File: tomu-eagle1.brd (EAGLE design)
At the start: 14.4 x 9.7 mm, 18 parts, among them U1 EFM32HG309F64G

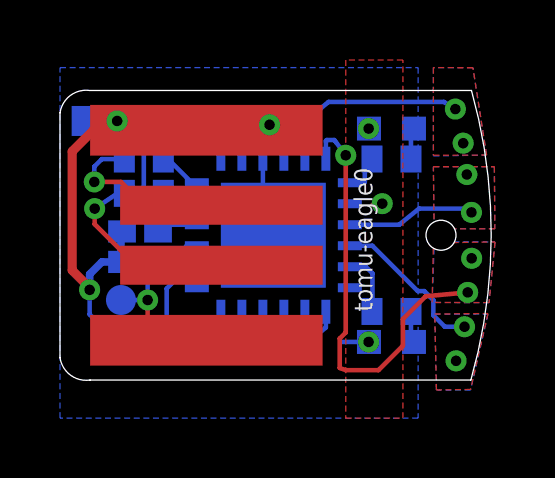
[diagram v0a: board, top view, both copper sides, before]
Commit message: added tomu-eagle1, more faithful to original tomu 0.4
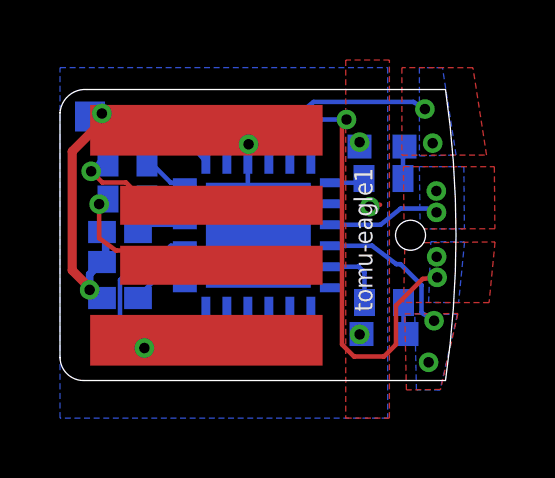
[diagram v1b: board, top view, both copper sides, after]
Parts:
- moved 5V 1.61 mm to (1.68, 2.12), turned to 180 degrees
- moved C1 1.24 mm to (2.00, 3.75)
- moved R1 0.70 mm to (10.8, 7.73)
- moved LED2 0.68 mm to (10.7, 8.80)
- moved C2 0.67 mm to (2.00, 5.95)
- moved C3 0.67 mm to (2.00, 4.95)
- moved R3 0.58 mm to (2.25, 7.05)
- moved R4 0.56 mm to (2.25, 8.25)
- moved U1 0.50 mm to (6.61, 5.84)
- moved D 0.41 mm to (5.57, 9.62)
- moved R2 0.39 mm to (10.8, 3.60)
- moved LED1 0.36 mm to (10.8, 2.55)
- moved C 0.19 mm to (3.27, 9.62)
- moved - 0.19 mm to (1.00, 9.80)
- moved R 0.10 mm to (4.83, 2.06)
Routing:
- net GND: track 25.6 -> 21.0 mm
- net DECOUPLE: track 3.30 -> 2.28 mm
- net +3V3: track 6.05 -> 5.12 mm
- net DBG_SWCLK: track 3.02 -> 2.14 mm
- net CAP1B: track 14.6 -> 15.4 mm
- net VUSB: track 7.46 -> 8.16 mm
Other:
- board size 14.4 x 9.7 mm -> 13.2 x 9.7 mm
- board text added: "tomu-eagle1"
- board text removed: "tomu-eagle0"

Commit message: fixes to tomu-eagle1
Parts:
- C1: device adafruit:C0402K -> adafruit:C0402
- moved LED1 0.05 mm to (10.8, 2.55)
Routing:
- net CAP1B: track 15.4 -> 14.3 mm
- net CAP0B: track 6.14 -> 6.26 mm, vias 2 -> 3
- net CAP1A: vias 2 -> 3
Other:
- outline, holes or cut-outs redrawn

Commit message: more fixes to tomu-eagle1
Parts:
- moved R2 0.21 mm to (10.8, 3.80)
- moved LED1 0.20 mm to (10.8, 2.75)

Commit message: more fixes, update readme
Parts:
- C2, C3: device adafruit:C0402K -> adafruit:C0402
- moved 5V 0.60 mm to (1.08, 2.12)
- moved C1 0.20 mm to (2.00, 3.55)
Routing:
- net VUSB: track 8.16 -> 8.71 mm
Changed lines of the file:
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@@
 <layer number="28" name="bValues" color="7" fill="1" visible="no" active="yes"/>
 <layer number="29" name="tStop" color="7" fill="3" visible="no" active="yes"/>
-<layer number="30" name="bStop" color="7" fill="6" visible="no" active="yes"/>
+<layer number="30" name="bStop" color="7" fill="6" visible="yes" active="yes"/>
 <layer number="31" name="tCream" color="7" fill="4" visible="no" active="yes"/>
 <layer number="32" name="bCream" color="7" fill="5" visible="no" active="yes"/>
@@
 <hole x="11.684" y="5.842" drill="1.2"/>
 <polygon width="0.1524" layer="29">
-<vertex x="12.192" y="11.684"/>
+<vertex x="11.392" y="11.684"/>
 <vertex x="14.986" y="11.684"/>
 <vertex x="14.986" y="0"/>
-<vertex x="12.192" y="0"/>
+<vertex x="11.392" y="0"/>
 </polygon>
 <polygon width="0.1524" layer="30">
@@
 </autorouter>
 <elements>
-<element name="C1" library="adafruit" library_urn="urn:adsk.eagle:library:420" package="C0402" value="1uF" x="2" y="3.75" smashed="yes" rot="MR0">
-<attribute name="NAME" x="0.922" y="3.463" size="0.6096" layer="26" ratio="12" rot="MR0"/>
-<attribute name="VALUE" x="2.5" y="2.3" size="1.016" layer="28" rot="MR0"/>
-</element>
-<element name="C2" library="adafruit" library_urn="urn:adsk.eagle:library:420" package="C0402K" value="1uF" x="2" y="5.95" smashed="yes" rot="MR0">
+<element name="C1" library="adafruit" library_urn="urn:adsk.eagle:library:420" package="C0402" value="1uF" x="2" y="3.55" smashed="yes" rot="MR0">
+<attribute name="NAME" x="0.922" y="3.063" size="0.6096" layer="26" ratio="12" rot="MR0"/>
+<attribute name="VALUE" x="2.5" y="2.1" size="1.016" layer="28" rot="MR0"/>
+</element>
+<element name="C2" library="adafruit" library_urn="urn:adsk.eagle:library:420" package="C0402" value="1uF" x="2" y="5.95" smashed="yes" rot="MR0">
 <attribute name="NAME" x="0.872" y="5.613" size="0.6096" layer="26" ratio="12" rot="MR0"/>
 <attribute name="VALUE" x="2.5" y="4.5" size="1.016" layer="28" rot="MR0"/>
 </element>
-<element name="C3" library="adafruit" library_urn="urn:adsk.eagle:library:420" package="C0402K" value="4.7uF" x="2" y="4.95" smashed="yes" rot="MR0">
-<attribute name="NAME" x="0.872" y="4.663" size="0.6096" layer="26" ratio="12" rot="MR0"/>
-<attribute name="VALUE" x="2.5" y="3.5" size="1.016" layer="28" rot="MR0"/>
+<element name="C3" library="adafruit" library_urn="urn:adsk.eagle:library:420" package="C0402" value="4.7uF" x="2" y="4.9" smashed="yes" rot="MR0">
+<attribute name="NAME" x="0.872" y="4.613" size="0.6096" layer="26" ratio="12" rot="MR0"/>
+<attribute name="VALUE" x="2.5" y="3.45" size="1.016" layer="28" rot="MR0"/>
 </element>
 <element name="LED1" library="adafruit" library_urn="urn:adsk.eagle:library:420" package="CHIP-LED0603" value="grn" x="10.75" y="2.75" smashed="yes" rot="MR90">
@@
 </element>
 <element name="R3" library="adafruit" library_urn="urn:adsk.eagle:library:420" package="R0402" value="15" x="2.25" y="7.05" smashed="yes" rot="MR0">
-<attribute name="NAME" x="1.207" y="6.796" size="0.6096" layer="26" ratio="12" rot="MR0"/>
+<attribute name="NAME" x="1.207" y="6.996" size="0.6096" layer="26" ratio="12" rot="MR0"/>
 </element>
 <element name="R4" library="adafruit" library_urn="urn:adsk.eagle:library:420" package="R0402" value="15" x="2.25" y="8.25" smashed="yes" rot="MR0">
-<attribute name="NAME" x="1.157" y="7.996" size="0.6096" layer="26" ratio="12" rot="MR0"/>
+<attribute name="NAME" x="1.157" y="8.196" size="0.6096" layer="26" ratio="12" rot="MR0"/>
 </element>
 <element name="U1" library="todstuff" package="QFN24PAD" value="EFM32HG309F64G" x="6.612" y="5.842" smashed="yes" rot="MR0">
@@
 </element>
 <element name="T" library="testpad" library_urn="urn:adsk.eagle:library:385" package="TP10R" package3d_urn="urn:adsk.eagle:package:27959/1" value="TPTP10R" x="6.604" y="2.109" smashed="yes" rot="MR0">
-<attribute name="NAME" x="6.015" y="1.4931" size="0.8128" layer="26" ratio="12" rot="MR0"/>
+<attribute name="NAME" x="6" y="1.6" size="0.8128" layer="26" ratio="12" rot="MR0"/>
 <attribute name="TP_SIGNAL_NAME" value="" x="6.604" y="0.204" size="1" layer="38" rot="MR0"/>
 </element>
 <element name="R" library="testpad" library_urn="urn:adsk.eagle:library:385" package="TP10R" package3d_urn="urn:adsk.eagle:package:27959/1" value="TPTP10R" x="4.826" y="2.059" smashed="yes" rot="MR0">
-<attribute name="NAME" x="3.983" y="1.4431" size="0.8128" layer="26" ratio="12" rot="MR0"/>
+<attribute name="NAME" x="4" y="1.6" size="0.8128" layer="26" ratio="12" rot="MR0"/>
 <attribute name="TP_SIGNAL_NAME" value="" x="4.826" y="0.154" size="1" layer="38" rot="MR0"/>
 </element>
@@
 </element>
 <element name="RS" library="testpad" library_urn="urn:adsk.eagle:library:385" package="TP10R" package3d_urn="urn:adsk.eagle:package:27959/1" value="TPTP10R" x="8.128" y="2.109" smashed="yes" rot="MR90">
-<attribute name="NAME" x="9.571" y="1.7471" size="0.6096" layer="26" ratio="12" rot="MR0"/>
+<attribute name="NAME" x="8.629" y="3.0529" size="0.6096" layer="26" ratio="12" rot="MR180"/>
 <attribute name="TP_SIGNAL_NAME" value="" x="6.223" y="2.109" size="1" layer="38" rot="MR90"/>
 </element>
-<element name="5V" library="testpad" library_urn="urn:adsk.eagle:library:385" package="TP10R" package3d_urn="urn:adsk.eagle:package:27959/1" value="TPTP10R" x="1.676" y="2.117" smashed="yes" rot="MR180">
-<attribute name="NAME" x="0.029" y="2.6789" size="0.8128" layer="26" ratio="12" rot="MR180"/>
-<attribute name="TP_SIGNAL_NAME" value="" x="1.676" y="4.022" size="1" layer="38" rot="MR180"/>
-<attribute name="VALUE" x="1.295" y="2.498" size="0.0254" layer="28" rot="MR180"/>
+<element name="5V" library="testpad" library_urn="urn:adsk.eagle:library:385" package="TP10R" package3d_urn="urn:adsk.eagle:package:27959/1" value="TPTP10R" x="1.076" y="2.117" smashed="yes" rot="MR180">
+<attribute name="NAME" x="2.85" y="1.8" size="0.75" layer="26" ratio="12" rot="MR0"/>
+<attribute name="TP_SIGNAL_NAME" value="" x="1.076" y="4.022" size="1" layer="38" rot="MR180"/>
+<attribute name="VALUE" x="0.695" y="2.498" size="0.0254" layer="28" rot="MR180"/>
 </element>
 <element name="U$1" library="todstuff" package="USB-A-PCB-2" value="USBPCB2" x="6.35" y="5.842" smashed="yes">
@@
 <wire x1="2.088" y1="9.342" x2="4.445" y2="9.342" width="0.254" layer="1"/>
 <wire x1="0.9878" y1="4.2192" x2="0.9878" y2="4.0218" width="0.254" layer="1"/>
-<wire x1="1.4" y1="4.95" x2="1.397" y2="4.953" width="0.254" layer="16"/>
+<wire x1="1.35" y1="4.9" x2="1.397" y2="4.953" width="0.254" layer="16"/>
 <wire x1="1.524" y1="4.953" x2="1.397" y2="4.953" width="0.254" layer="16"/>
 <wire x1="0.9878" y1="4.5438" x2="0.9878" y2="4.0218" width="0.254" layer="16"/>
 <wire x1="1.397" y1="4.953" x2="0.9878" y2="4.5438" width="0.254" layer="16"/>
-<wire x1="1.4" y1="5.95" x2="1.524" y2="5.934" width="0.254" layer="16"/>
+<wire x1="1.35" y1="5.95" x2="1.524" y2="5.934" width="0.254" layer="16"/>
 <wire x1="1.524" y1="5.934" x2="1.524" y2="4.953" width="0.254" layer="16"/>
 <wire x1="0.9878" y1="4.0218" x2="0.9878" y2="4.0922" width="0.3048" layer="1"/>
@@
 <wire x1="0.4064" y1="8.636" x2="1.1124" y2="9.342" width="0.3048" layer="1"/>
 <wire x1="1.1124" y1="9.342" x2="1.214" y2="9.342" width="0.3048" layer="1"/>
-<wire x1="1.35" y1="3.75" x2="1.0696" y2="3.94" width="0.1524" layer="16"/>
+<wire x1="1.35" y1="3.55" x2="1.0696" y2="3.94" width="0.1524" layer="16"/>
 <wire x1="1.0696" y1="3.94" x2="0.9878" y2="4.0218" width="0.1524" layer="16"/>
 </signal>
@@
 <wire x1="3.358" y1="2.342" x2="4.88" y2="2.342" width="0.1524" layer="1"/>
 <wire x1="2.813" y1="2.083" x2="3.121" y2="2.213" width="0.1524" layer="1"/>
-<wire x1="2.6" y1="4.95" x2="3.2" y2="5" width="0.1524" layer="16"/>
+<wire x1="2.65" y1="4.9" x2="3.2" y2="5" width="0.1524" layer="16"/>
 <wire x1="3.692" y1="5.492" x2="4.162" y2="5.492" width="0.1524" layer="16"/>
 <wire x1="3.2" y1="5" x2="3.692" y2="5.492" width="0.1524" layer="16"/>
-<wire x1="1.676" y1="2.117" x2="1.71" y2="2.083" width="0.1524" layer="16"/>
+<wire x1="1.076" y1="2.117" x2="1.71" y2="2.083" width="0.1524" layer="16"/>
 <wire x1="1.71" y1="2.083" x2="2" y2="2.083" width="0.1524" layer="16"/>
 <wire x1="2" y1="2.083" x2="2.813" y2="2.083" width="0.1524" layer="16"/>
-<wire x1="2.6" y1="4.95" x2="2" y2="4.35" width="0.1524" layer="16"/>
+<wire x1="2.65" y1="4.9" x2="2" y2="4.35" width="0.1524" layer="16"/>
 <wire x1="2" y1="4.35" x2="2" y2="2.083" width="0.1524" layer="16"/>
 </signal>
@@
 <contactref element="U1" pad="14"/>
 <contactref element="C1" pad="1"/>
-<wire x1="4.162" y1="4.792" x2="3.592" y2="4.792" width="0.1524" layer="16"/>
-<wire x1="2.74" y1="3.94" x2="2.65" y2="3.75" width="0.1524" layer="16"/>
-<wire x1="3.592" y1="4.792" x2="3.2911" y2="4.4911" width="0.1524" layer="16"/>
-<wire x1="3.2911" y1="4.4911" x2="3.2911" y2="4.4853125" width="0.1524" layer="16"/>
-<wire x1="2.578" y1="3.7722125" x2="2.65" y2="3.75" width="0.1524" layer="16"/>
-<wire x1="3.2911" y1="4.4853125" x2="2.578" y2="3.7722125" width="0.1524" layer="16"/>
+<wire x1="2.74" y1="3.94" x2="2.702246875" y2="3.776403125" width="0.1524" layer="16"/>
+<wire x1="2.702246875" y1="3.776403125" x2="2.65" y2="3.55" width="0.1524" layer="16"/>
+<wire x1="4.162" y1="4.792" x2="3.71784375" y2="4.792" width="0.1524" layer="16"/>
+<wire x1="3.71784375" y1="4.792" x2="2.702246875" y2="3.776403125" width="0.1524" layer="16"/>
 </signal>
 <signal name="+3V3">
@@
 <wire x1="10" y1="2.75" x2="9.987" y2="2.636" width="0.1524" layer="16"/>
 <via x="9.987" y="2.636" extent="1-16" drill="0.35"/>
-<wire x1="2.6" y1="5.95" x2="2.2" y2="6.6" width="0.1524" layer="16"/>
+<wire x1="2.65" y1="5.95" x2="2.2" y2="6.6" width="0.1524" layer="16"/>
 <wire x1="2.2" y1="6.6" x2="2.2" y2="7.2" width="0.1524" layer="16"/>
 <wire x1="4.162" y1="6.192" x2="2.792" y2="6.192" width="0.1524" layer="16"/>
